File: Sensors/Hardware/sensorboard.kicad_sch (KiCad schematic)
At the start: 74 parts, among them J1 RBUS, J2 Conn_Coaxial, U1 ESP32-S3, U2 LTC4411, U3 TPS61092RSAR, Y1 40MHz±10ppm

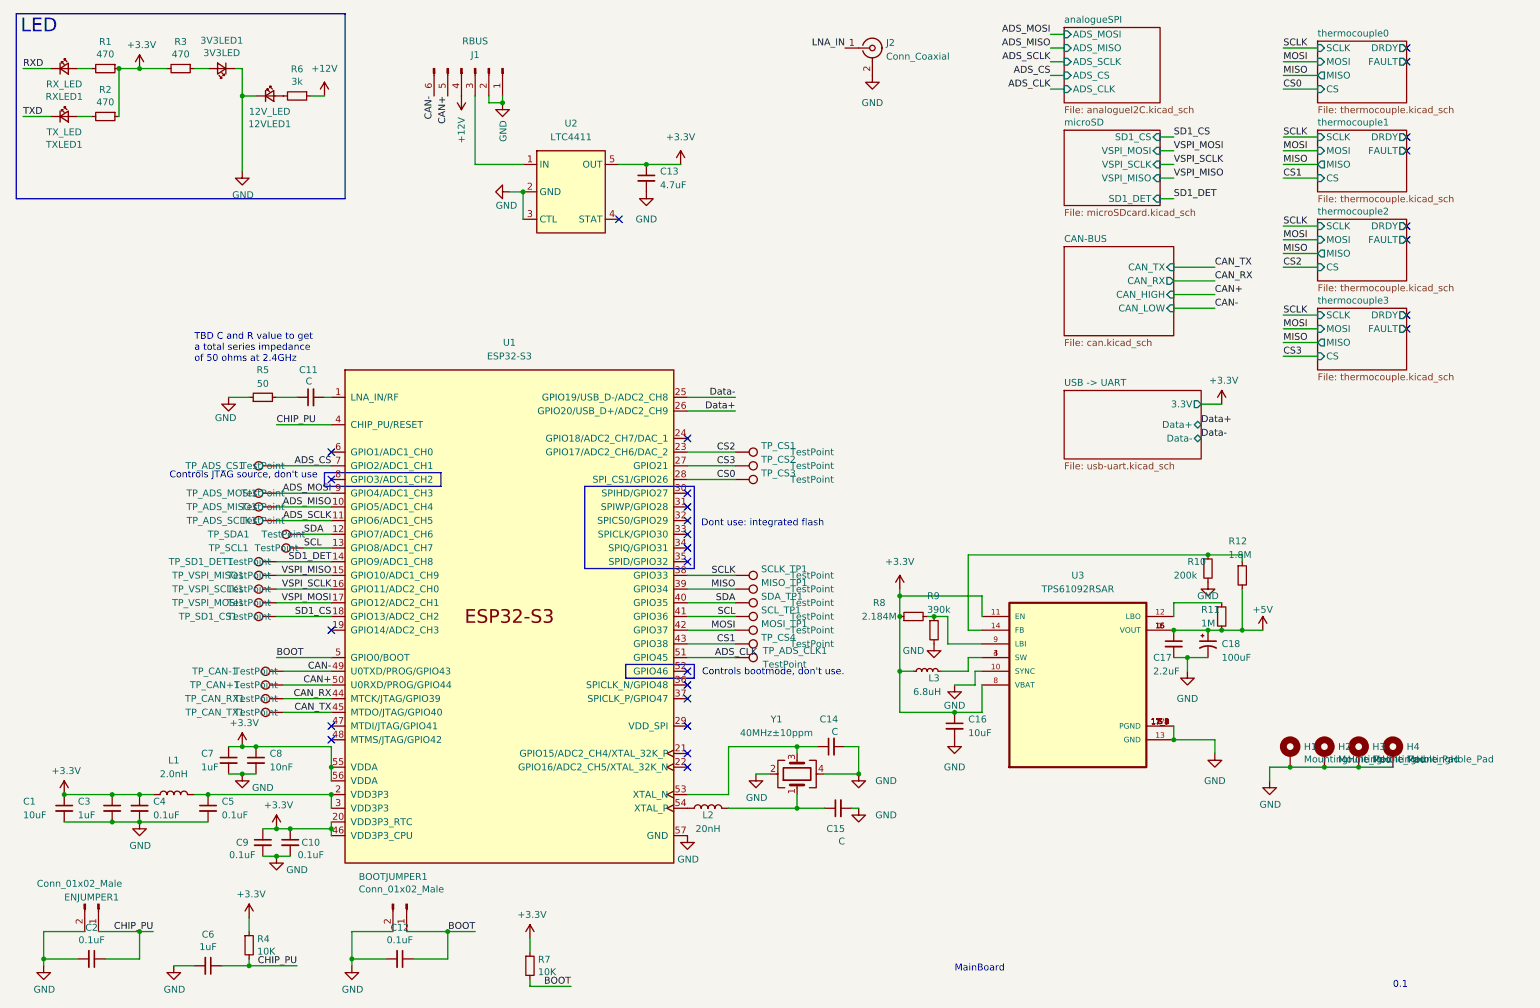
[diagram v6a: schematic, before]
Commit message: added 10V rail, moved to boosts sheet
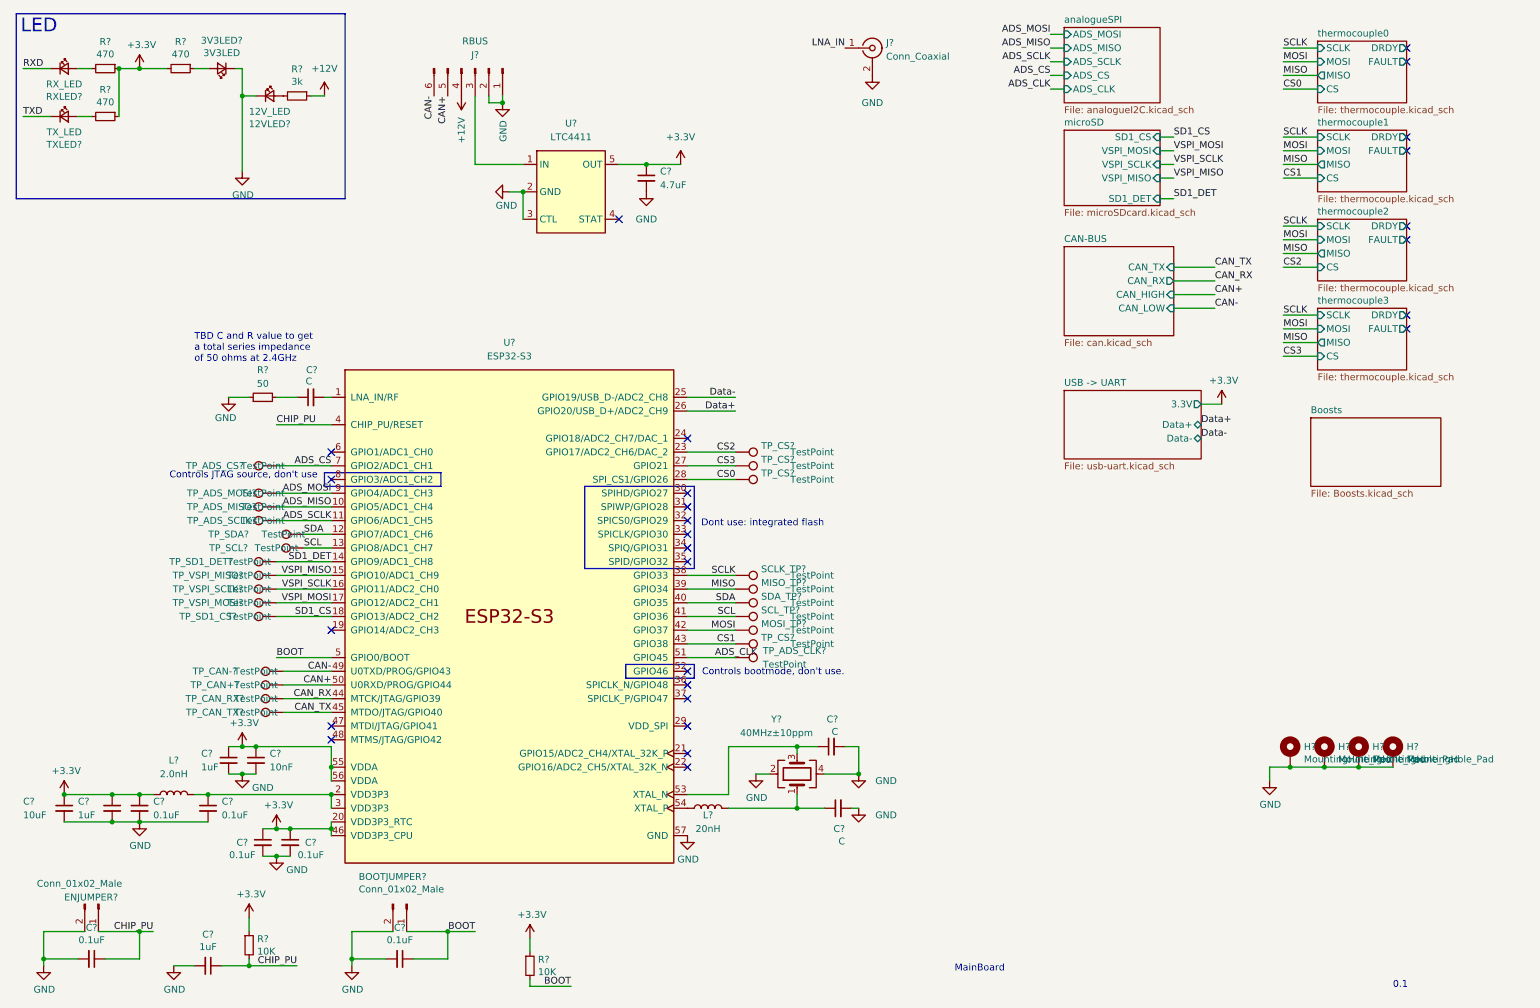
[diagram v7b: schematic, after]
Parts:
- removed C16: 10uF, Capacitor_SMD:C_0603_1608Metric, symbol Device:C_Small
- removed C17: 2.2uF, Capacitor_SMD:C_0603_1608Metric, symbol Device:C_Small
- removed C18: 100uF, iclr:CAPC2012X145N, symbol Device:C_Polarized_Small_US
- removed L3: 6.8uH, iclr:INDPM3030X200N, symbol Device:L_Small
- removed R10: 200k, Resistor_SMD:R_0603_1608Metric, symbol Device:R_Small
- removed R11: 1M, Resistor_SMD:R_0603_1608Metric, symbol Device:R_Small
- removed R12: 1.8M, Resistor_SMD:R_0603_1608Metric, symbol Device:R_Small
- removed R8: 2.184M, Resistor_SMD:R_0603_1608Metric, symbol Device:R_Small
- removed R9: 390k, Resistor_SMD:R_0603_1608Metric, symbol Device:R_Small
- removed U3: TPS61092RSAR, iclr:QFN65P400X400X100-17N, symbol iclr:TPS61092RSAR
- renumbered 12VLED1 to 12VLED?, 3V3LED1 to 3V3LED?, BOOTJUMPER1 to BOOTJUMPER?, C12 to C?, C4 to C?, C14 to C?, C7 to C?, C8 to C?, C10 to C?, C5 to C?, C2 to C?, C1 to C?, C11 to C?, C6 to C?, C3 to C?, C9 to C?, C15 to C?, C13 to C?, ENJUMPER1 to ENJUMPER?, H4 to H?, H3 to H?, H2 to H?, H1 to H?, J1 to J?, J2 to J?, L2 to L?, L1 to L?, MISO_TP1 to MISO_TP?, MOSI_TP1 to MOSI_TP?, R7 to R?, R6 to R?, R2 to R?, R4 to R?, R1 to R?, R5 to R?, R3 to R?, RXLED1 to RXLED?, SCLK_TP1 to SCLK_TP?, SCL_TP1 to SCL_TP?, SDA_TP1 to SDA_TP?, TP_ADS_CLK1 to TP_ADS_CLK?, TP_ADS_CS1 to TP_ADS_CS?, TP_ADS_MISO1 to TP_ADS_MISO?, TP_ADS_MOSI1 to TP_ADS_MOSI?, TP_ADS_SCLK1 to TP_ADS_SCLK?, TP_CAN+1 to TP_CAN+?, TP_CAN-1 to TP_CAN-?, TP_CAN_RX1 to TP_CAN_RX?, TP_CAN_TX1 to TP_CAN_TX?, TP_CS4 to TP_CS?, TP_CS1 to TP_CS?, TP_CS2 to TP_CS?, TP_CS3 to TP_CS?, TP_SCL1 to TP_SCL?, TP_SD1_CS1 to TP_SD1_CS?, TP_SD1_DET1 to TP_SD1_DET?, TP_SDA1 to TP_SDA?, TP_VSPI_MISO1 to TP_VSPI_MISO?, TP_VSPI_MOSI1 to TP_VSPI_MOSI?, TP_VSPI_SCLK1 to TP_VSPI_SCLK?, TXLED1 to TXLED?, U2 to U?, U1 to U?, Y1 to Y?
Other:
- added sheet Boosts (Boosts.kicad_sch)

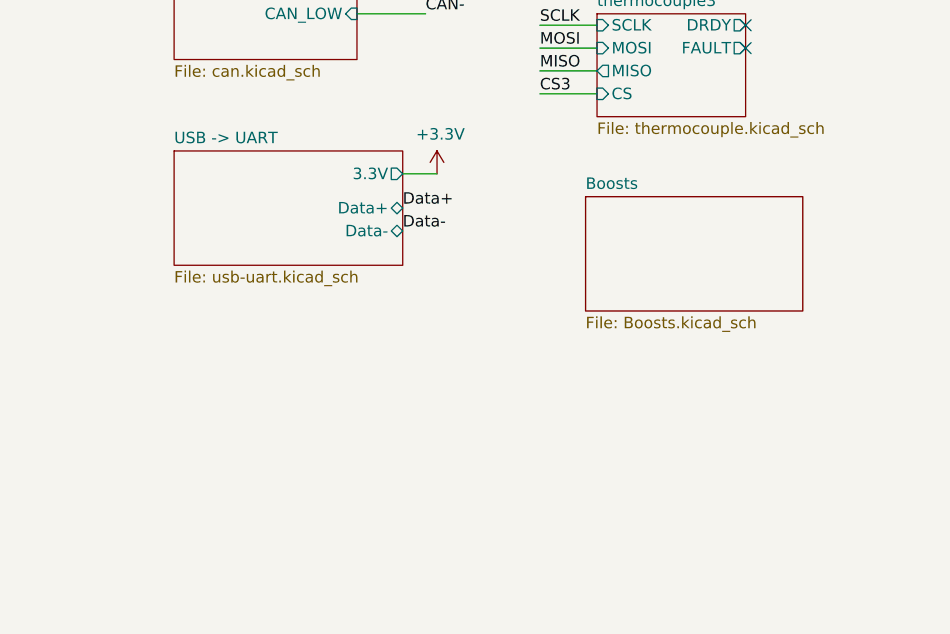
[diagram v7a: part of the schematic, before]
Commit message: update
still need to fix 10v rail
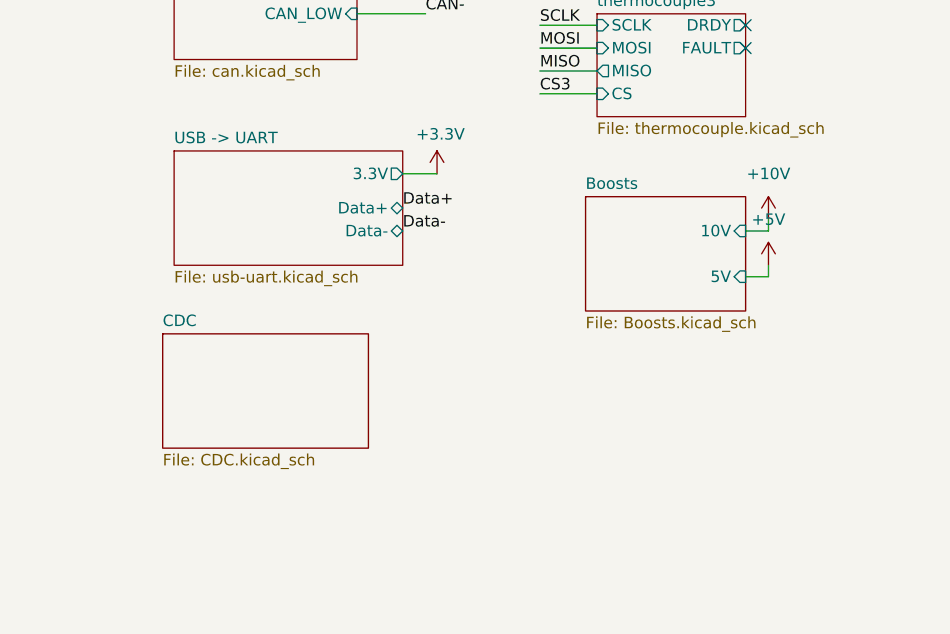
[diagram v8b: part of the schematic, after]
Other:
- added sheet CDC (CDC.kicad_sch)
- sheet Boosts ports: added 10V, 5V; removed none
